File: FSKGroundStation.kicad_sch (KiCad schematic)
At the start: 0 parts

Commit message: Finish layout
Signed-off-by: Corey Minyard <corey@minyard.net>
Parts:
- added H1, H2, H3, H4: M3 Mount (MTS-14 and 97790503111), MountingHole:MountingHole_3.2mm_M3, symbol Mechanical:MountingHole
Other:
- added sheet Diplexer (diplexer.kicad_sch)

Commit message: Add fiducials to the board
Signed-off-by: Corey Minyard <corey@minyard.net>
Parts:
- added FID1, FID2, FID3, FID4, FID5, FID6: Fiducial (round), Fiducial:Fiducial_1mm_Mask2mm, symbol Mechanical:Fiducial
- added FID10, FID11, FID12, FID7, FID8, FID9: Fiducial (square), footprints:Fiducial_Square_1mm_Mask2mm, symbol PACSAT_DEV_misc:Fiducial (square)

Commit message: Add fiduciaries and a control output
Signed-off-by: Corey Minyard <corey@minyard.net>
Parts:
- FID10, FID11, FID12, FID7, FID8, FID9: symbol PACSAT_DEV_misc:Fiducial (square) -> Local Connectors:Fiducial (square)
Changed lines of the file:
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@@
 	)
 	(symbol
-		(lib_id "PACSAT_DEV_misc:Fiducial (square)")
+		(lib_id "Local Connectors:Fiducial (square)")
 		(at 147.32 163.83 0)
 		(unit 1)
@@
 	)
 	(symbol
-		(lib_id "PACSAT_DEV_misc:Fiducial (square)")
+		(lib_id "Local Connectors:Fiducial (square)")
 		(at 147.32 151.13 0)
 		(unit 1)
@@
 	)
 	(symbol
-		(lib_id "PACSAT_DEV_misc:Fiducial (square)")
+		(lib_id "Local Connectors:Fiducial (square)")
 		(at 147.32 170.18 0)
 		(unit 1)
@@
 	)
 	(symbol
-		(lib_id "PACSAT_DEV_misc:Fiducial (square)")
+		(lib_id "Local Connectors:Fiducial (square)")
 		(at 147.32 182.88 0)
 		(unit 1)
@@
 	)
 	(symbol
-		(lib_id "PACSAT_DEV_misc:Fiducial (square)")
+		(lib_id "Local Connectors:Fiducial (square)")
 		(at 147.32 176.53 0)
 		(unit 1)
@@
 	)
 	(symbol
-		(lib_id "PACSAT_DEV_misc:Fiducial (square)")
+		(lib_id "Local Connectors:Fiducial (square)")
 		(at 147.32 157.48 0)
 		(unit 1)

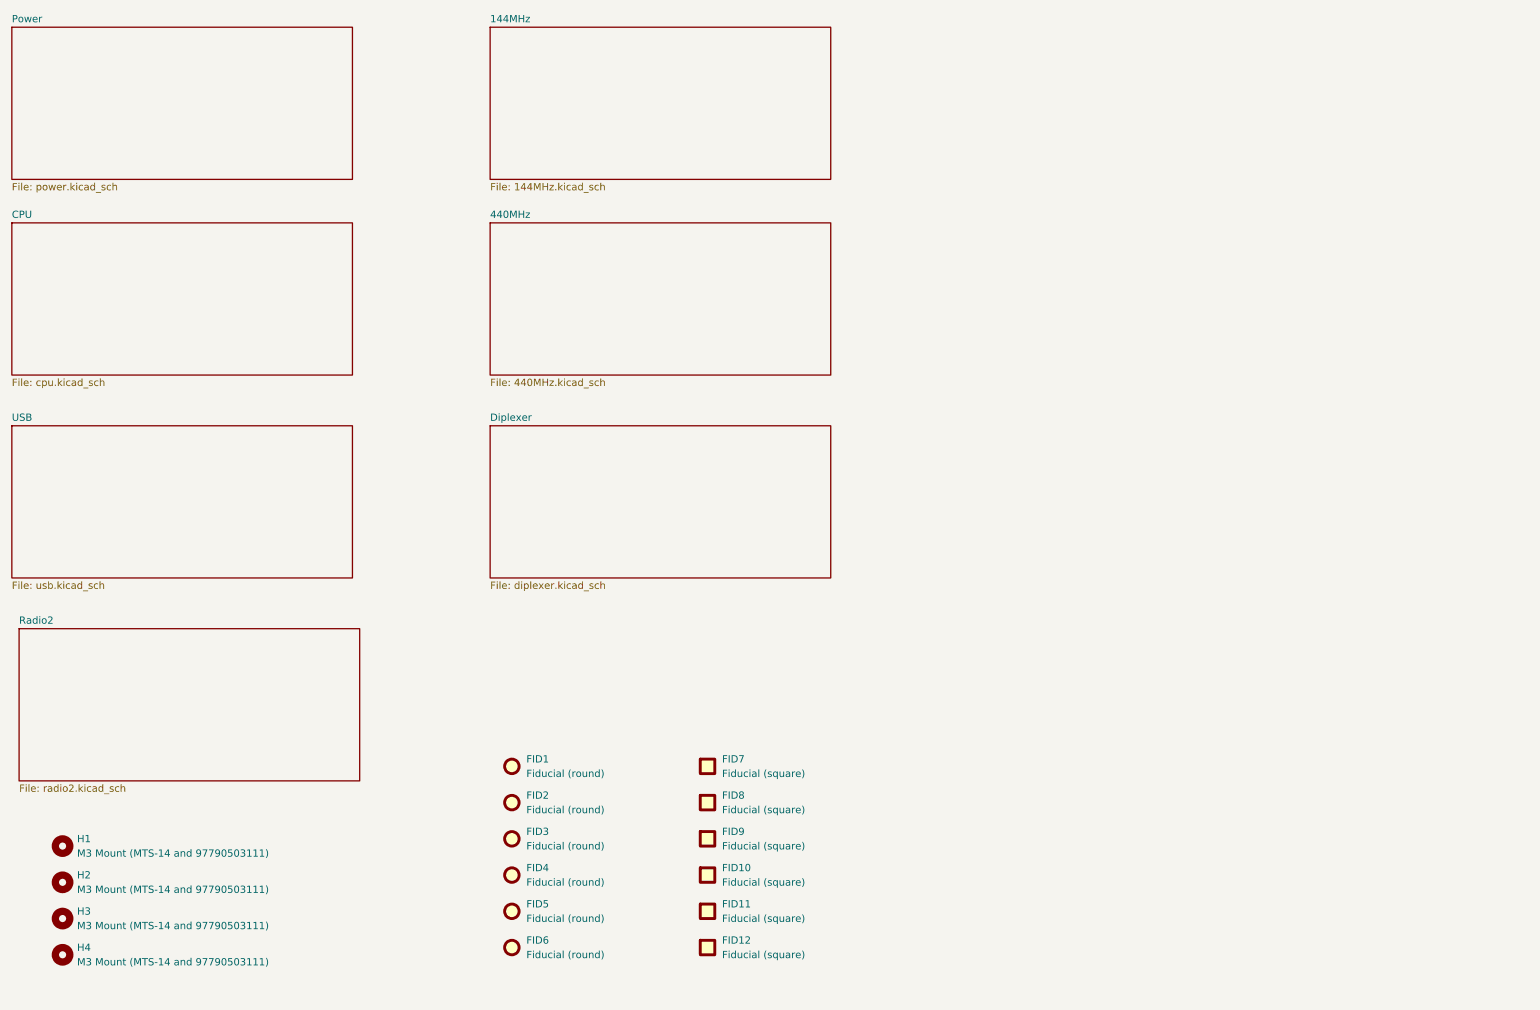
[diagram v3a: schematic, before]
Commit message: First start at reworking to get HDLC
Signed-off-by: Corey Minyard <corey@minyard.net>
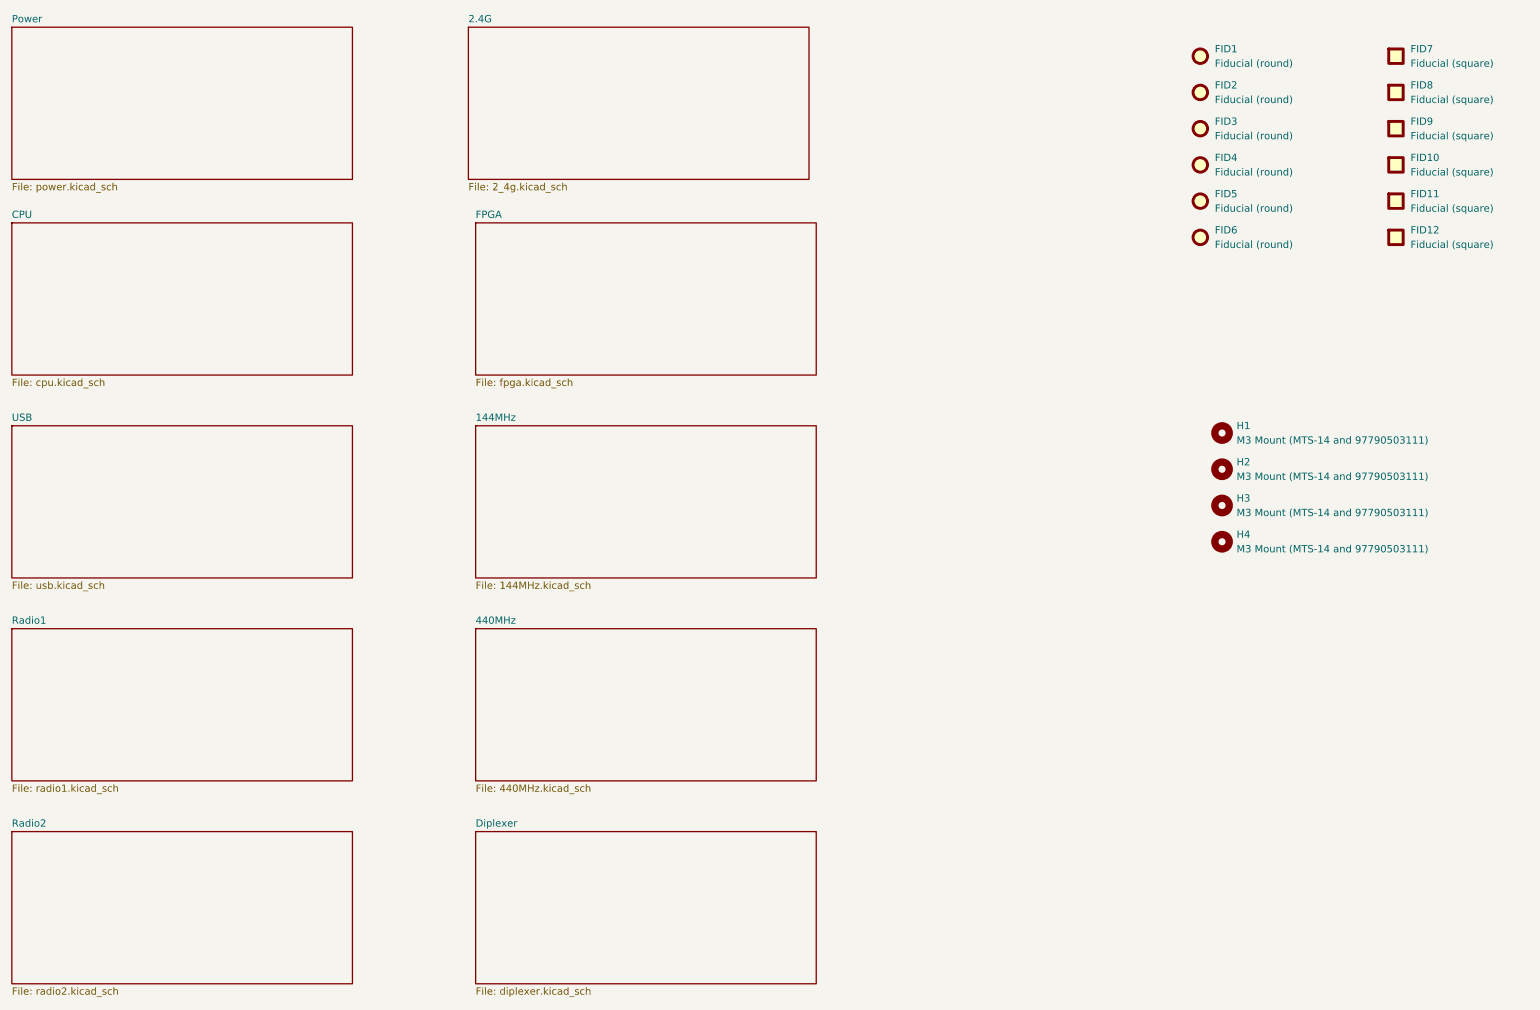
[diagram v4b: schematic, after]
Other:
- added sheet 2.4G (2_4g.kicad_sch)
- added sheet FPGA (fpga.kicad_sch)
- added sheet Radio1 (radio1.kicad_sch)
- moved on the sheet: FID1, FID10, FID11, FID12, FID2, FID3, FID4, FID5, FID6, FID7, FID8, FID9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
